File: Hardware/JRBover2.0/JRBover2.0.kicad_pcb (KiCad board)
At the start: 2 copper layers, 50 x 50 mm, 25 parts, among them J1 EncoderMotorDerecha, J10 Input of Driver L9110, J2 HC_SRO4, J3 HC_SRO4, J4 HC_SRO4, J5 CableAlimentacion, J6 SWITCH, J7 Programador, J8 BOTON, J9 EncoderMotorIzquierda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

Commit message: en correcion por bustos, ya casi
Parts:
- moved H2 59.3 mm to (157.4, 120.8)
- moved R2 47.8 mm to (153.3, 105.3), turned to 180 degrees
- moved C5 42.3 mm to (151.7, 101.6), turned to 90 degrees
- moved H1 41.7 mm to (121.3, 78.0)
- moved LED2 40.4 mm to (148.9, 104.5), turned to 90 degrees
- moved C6 33.0 mm to (148.4, 98.9), turned to -90 degrees
- moved J8 7.93 mm to (130.1, 79.4)
- moved J9 5.57 mm to (142.2, 79.4)
- moved C4 5.56 mm to (143.0, 114.3), turned to -90 degrees
- moved J4 3.78 mm to (156.0, 84.9)
- moved C2 3.76 mm to (131.8, 115.8)
- moved C3 3.76 mm to (140.5, 119.7)
- moved LED1 3.76 mm to (146.9, 119.1)
- moved R1 3.76 mm to (147.0, 115.7)
- moved U2 3.76 mm to (136.3, 117.5)
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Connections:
- U1 pad 13: /D0 -> unconnected-(U1-Pad13)
- U1 pad 14: /OUT_IR1 -> /D0
- U1 pad 29: /IN3 -> unconnected-(U1-Pad29)
- U1 pad 30: /IN4 -> unconnected-(U1-Pad30)
- U1 pad 36: unconnected-(U1-Pad36) -> /IN3
- U1 pad 37: unconnected-(U1-Pad37) -> /IN4
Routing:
- net GND: track 0.00 -> 192.5 mm
- net +5V: track 0.00 -> 145.2 mm
- net +3V3: track 0.00 -> 37.4 mm
- net /IN1: track 0.00 -> 20.2 mm
- net +7.5V: track 0.00 -> 19.6 mm
- net /IN2: track 0.00 -> 18.8 mm
- net /Trig1: track 0.00 -> 15.0 mm
- net /Trig3: track 0.00 -> 14.5 mm
- net /Trig2: track 0.00 -> 14.5 mm
- net /IN4: track 0.00 -> 14.4 mm
- net /D0: track 0.00 -> 13.4 mm
- net /IN3: track 0.00 -> 13.2 mm
- net /Echo3: track 0.00 -> 11.4 mm
- net /Echo: track 0.00 -> 11.3 mm
- net /Echo2: track 0.00 -> 10.7 mm
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
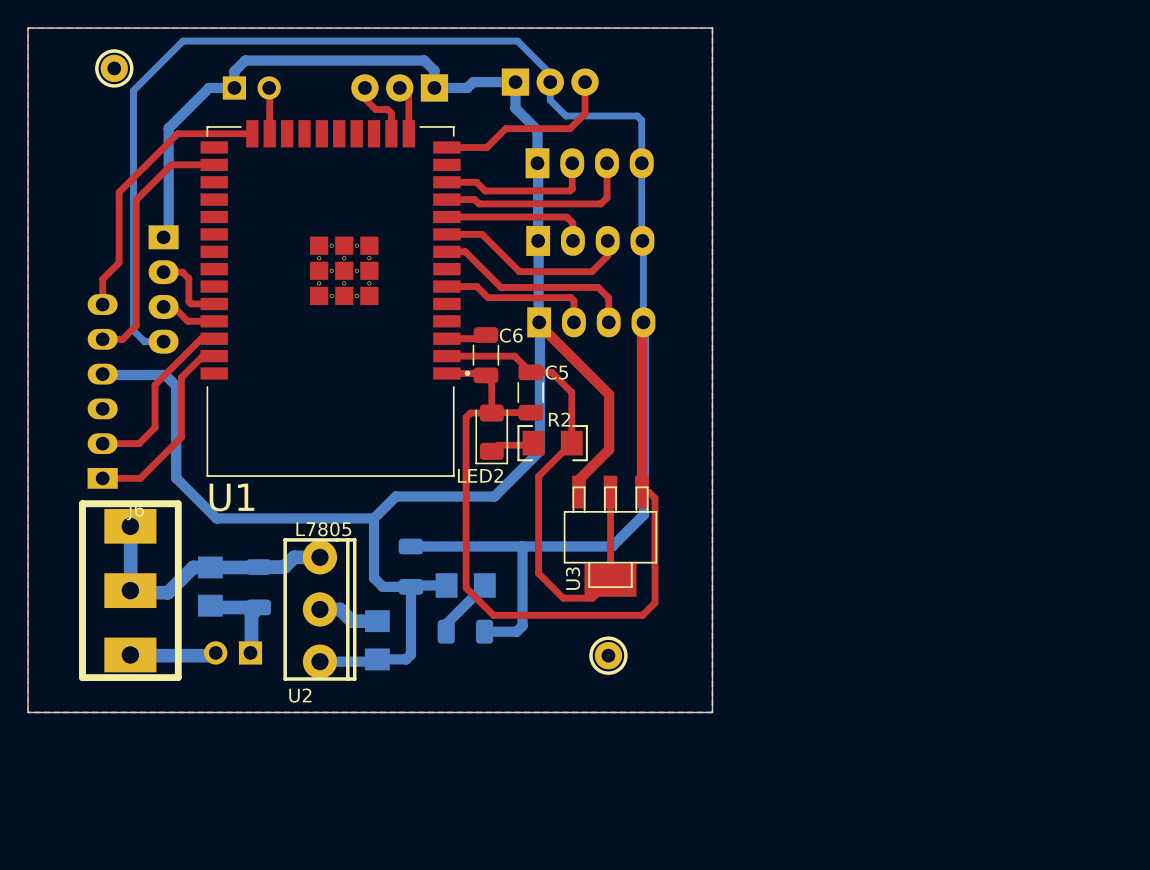
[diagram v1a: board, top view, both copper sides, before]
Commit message: el anterior tenia erro de antena esp32 , esta vez esta en la orilla espera correccion:)
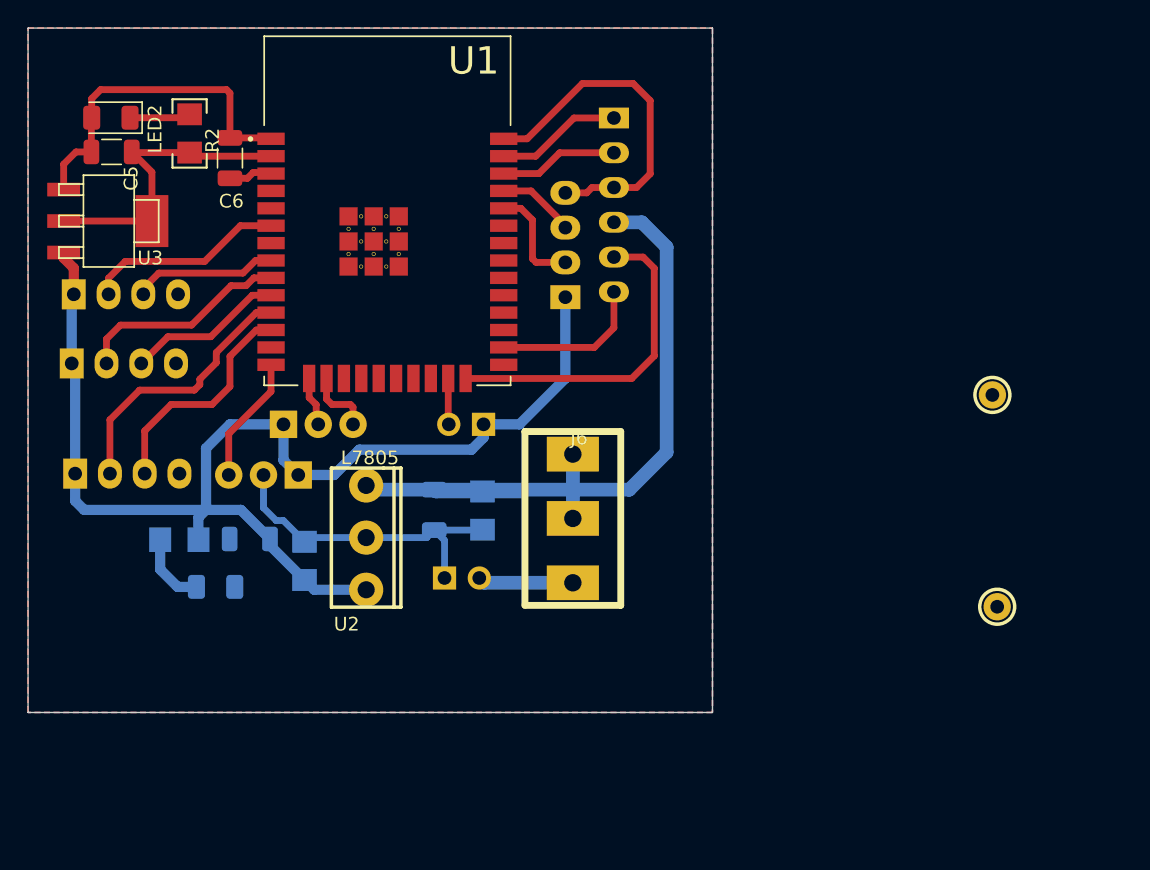
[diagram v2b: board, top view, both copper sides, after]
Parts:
- moved H1 68.4 mm to (185.4, 101.8), turned to 180 degrees
- moved U3 43.3 mm to (120.9, 89.1), turned to -90 degrees
- moved J4 40.7 mm to (122.2, 107.5)
- moved J10 39.8 mm to (157.8, 87.9), turned to -90 degrees
- moved LED2 36.1 mm to (121.0, 81.5), turned to 180 degrees
- moved J1 35.5 mm to (132.2, 107.7), turned to 180 degrees
- moved C5 35.3 mm to (121.1, 84.0), turned to 0 degrees
- moved J3 35.2 mm to (122.0, 99.5)
- moved R2 34.9 mm to (126.8, 82.7), turned to 90 degrees
- moved J2 34.1 mm to (122.2, 94.5)
- moved J6 32.8 mm to (154.8, 110.8)
- moved J8 30.6 mm to (148.3, 104.0), turned to 90 degrees
- moved J7 29.5 mm to (154.2, 90.8), turned to 90 degrees
- moved H2 28.6 mm to (185.8, 117.3)
- moved J9 25.3 mm to (136.2, 104.0), turned to 0 degrees
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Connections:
- J10 pad 4: +5V -> +7.5V
- U1 pad 10: /Echo2 -> /Trig2
- U1 pad 11: /Trig3 -> /Echo3
- U1 pad 12: /Echo3 -> /Trig3
- U1 pad 24: /IN1 -> /IN2
- U1 pad 26: /IN2 -> /IN1
- U1 pad 9: /Trig2 -> /Echo2
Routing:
- net GND: track 192.5 -> 77.2 mm
- net +5V: track 145.2 -> 89.2 mm
- net +7.5V: track 19.6 -> 53.9 mm
- net +3V3: track 37.4 -> 22.4 mm
- net /IN1: track 20.2 -> 11.3 mm
- net /Echo3: track 11.4 -> 19.6 mm
- net /IN2: track 18.8 -> 24.2 mm
- net /IN4: track 14.4 -> 9.21 mm
- net /Echo2: track 10.7 -> 15.7 mm
- net /IN3: track 13.2 -> 8.68 mm
- net /Trig1: track 15.0 -> 10.6 mm
- net /D0: track 13.4 -> 9.33 mm
- net /Echo: track 11.3 -> 14.6 mm
- net /Trig2: track 14.5 -> 11.5 mm
- net /Trig3: track 14.5 -> 16.7 mm
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
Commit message: la perfeccione y le agregue Letra, no me hace la malla GND raro:)
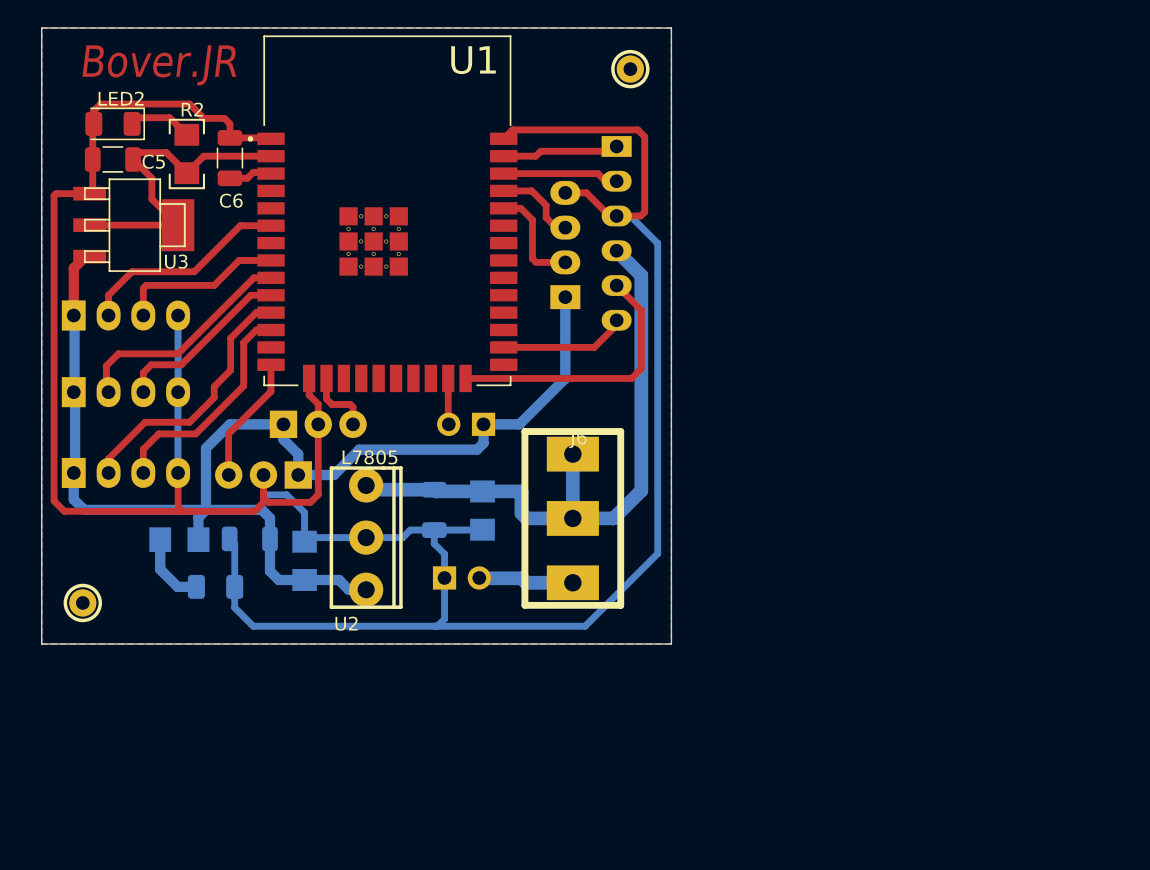
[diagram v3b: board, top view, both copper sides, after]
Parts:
- moved H2 66.8 mm to (119.0, 117.0)
- moved H1 35.6 mm to (159.0, 78.0)
- moved J3 2.11 mm to (122.2, 101.6)
- moved J10 2.09 mm to (158.0, 90.0)
- moved U3 1.92 mm to (122.8, 89.4)
- moved J2 1.55 mm to (122.2, 96.0)
- moved R2 1.51 mm to (126.6, 84.2)
- moved C5 0.56 mm to (121.2, 84.6)
- moved LED2 0.47 mm to (121.2, 82.0)
- moved J4 0.11 mm to (122.2, 107.5)
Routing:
- net GND: track 77.2 -> 209.6 mm
- net +7.5V: track 53.9 -> 45.8 mm
- net /IN2: track 24.2 -> 20.0 mm
- net +5V: track 89.2 -> 91.5 mm
- net /IN1: track 11.3 -> 9.28 mm
- net +3V3: track 22.4 -> 24.0 mm
- net /Trig1: track 10.6 -> 12.2 mm
- net /Trig2: track 11.5 -> 13.1 mm
- net /Echo2: track 15.7 -> 16.7 mm
- net /Echo: track 14.6 -> 15.5 mm
- net /IN4: track 9.21 -> 8.54 mm
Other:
- board size 50 x 50 mm -> 46 x 45 mm
- board text added: "Bover.JR"
- board text added: "x2"
